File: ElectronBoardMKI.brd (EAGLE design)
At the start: 88.9 x 202.9 mm, 36 parts, among them IC1 7805TV, Q1 TN0602N3, Q2 TN0602N3, T2 2N2222, T3 2N2222, T4 2N2222

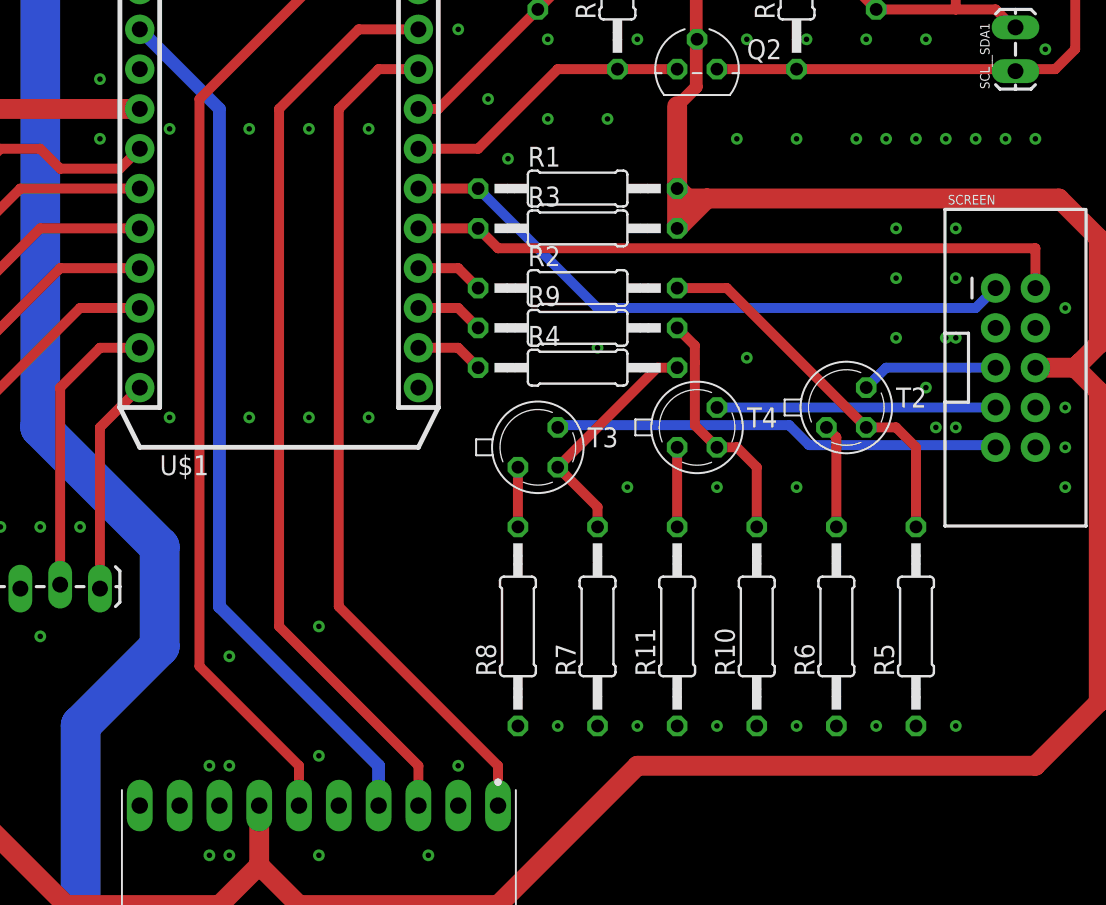
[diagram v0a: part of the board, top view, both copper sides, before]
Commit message: Net Lables + Pull-Down Resistors on Electron
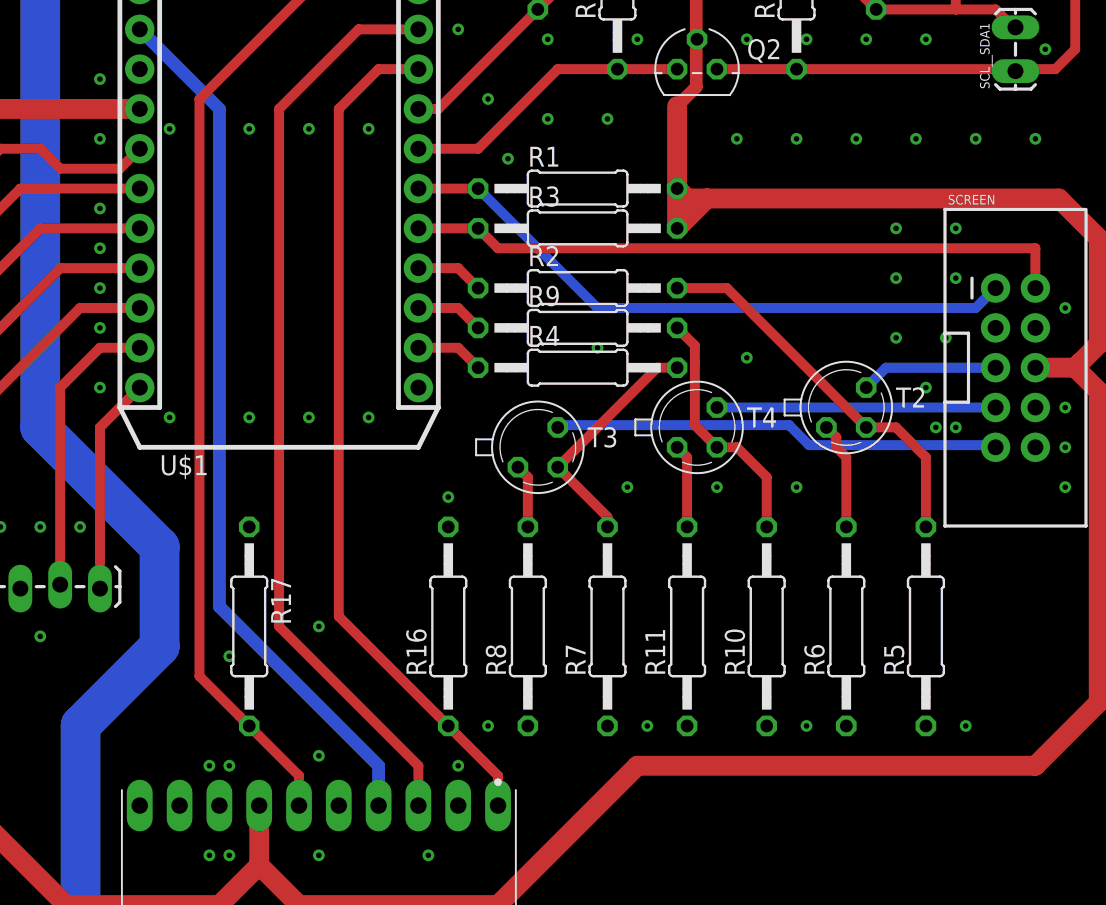
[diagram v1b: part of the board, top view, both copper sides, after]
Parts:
- added R16, R17: 47k, resistor:0207/12
- moved R10 0.64 mm to (64.1, 66.0)
- moved R5 0.64 mm to (74.3, 66.0)
- moved R6 0.64 mm to (69.2, 66.0)
- moved R8 0.64 mm to (48.9, 66.0)
- moved R11 0.63 mm to (59.1, 66.0)
- moved R7 0.63 mm to (54.0, 66.0)
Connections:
- net N$10 renamed COOLING-OUTB
- net N$11 renamed BLUE-NPN-BASE
- net N$12 renamed BLUE-NPN-EMITTER
- net N$13 renamed RED-NPN-BASE
- net N$14 renamed RED-NPN-EMITTER
- net N$15 renamed GREEN-NPN-BASE
- net N$16 renamed GREEN-NPN-EMITTER
- net N$9 renamed COOLING-OUTA
- net COOLING-INA: now also R16.1
- net COOLING-INB: now also R17.2
- net GND: now also R16.2, R17.1
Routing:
- net COOLING-INB: track 64.6 -> 65.5 mm

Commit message: Holes
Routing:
- net 3V3: track 337.0 -> 333.2 mm
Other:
- board size 88.9 x 202.9 mm -> 88 x 202.9 mm
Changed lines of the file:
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@@
 <setting verticaltext="up"/>
 </settings>
-<grid distance="0.025" unitdist="inch" unit="inch" style="lines" multiple="1" display="no" altdistance="5" altunitdist="mil" altunit="mil"/>
+<grid distance="25" unitdist="mil" unit="mil" style="lines" multiple="1" display="no" altdistance="5" altunitdist="mil" altunit="mil"/>
 <layers>
 <layer number="1" name="Top" color="4" fill="1" visible="yes" active="yes"/>
@@
 <layer number="43" name="vRestrict" color="2" fill="10" visible="yes" active="yes"/>
 <layer number="44" name="Drills" color="7" fill="1" visible="no" active="yes"/>
-<layer number="45" name="Holes" color="7" fill="1" visible="no" active="yes"/>
+<layer number="45" name="Holes" color="7" fill="1" visible="yes" active="yes"/>
 <layer number="46" name="Milling" color="3" fill="1" visible="no" active="yes"/>
 <layer number="47" name="Measures" color="7" fill="1" visible="no" active="yes"/>
@@
 <board>
 <plain>
-<wire x1="0" y1="0" x2="88.88" y2="0" width="0" layer="20"/>
-<wire x1="88.88" y1="0" x2="88.88" y2="202.87" width="0" layer="20"/>
-<wire x1="88.88" y1="202.87" x2="0" y2="202.87" width="0" layer="20"/>
+<wire x1="0" y1="0" x2="88" y2="0" width="0" layer="20"/>
+<wire x1="88" y1="0" x2="88" y2="200" width="0" layer="20"/>
+<wire x1="88" y1="200" x2="0" y2="202.87" width="0" layer="20"/>
 <wire x1="0" y1="202.87" x2="0" y2="0" width="0" layer="20"/>
+<hole x="6.15" y="6.15" drill="4"/>
+<hole x="78.05" y="6.15" drill="4"/>
+<hole x="6.15" y="193.85" drill="4"/>
+<hole x="78.05" y="193.85" drill="4"/>
+<hole x="6.15" y="150" drill="4"/>
+<hole x="78.05" y="150" drill="4"/>
 </plain>
 <attributes>
@@
 <via x="72.39" y="91.44" extent="1-16" drill="0.35"/>
 <via x="75.565" y="84.455" extent="1-16" drill="0.35"/>
-<via x="83.185" y="86.36" extent="1-16" drill="0.35"/>
-<via x="83.185" y="74.93" extent="1-16" drill="0.35"/>
-<via x="83.185" y="77.47" extent="1-16" drill="0.35"/>
-<via x="83.185" y="80.01" extent="1-16" drill="0.35"/>
+<via x="82.8675" y="86.36" extent="1-16" drill="0.35"/>
+<via x="82.8675" y="74.93" extent="1-16" drill="0.35"/>
+<via x="82.8675" y="77.47" extent="1-16" drill="0.35"/>
+<via x="82.8675" y="80.01" extent="1-16" drill="0.35"/>
 <via x="76.835" y="59.69" extent="1-16" drill="0.35"/>
 <via x="66.675" y="59.69" extent="1-16" drill="0.35"/>
@@
 <via x="24.13" y="45.72" extent="1-16" drill="0.35"/>
 <via x="39.37" y="45.72" extent="1-16" drill="0.35"/>
-<via x="3.175" y="86.36" extent="1-16" drill="0.35"/>
+<via x="3.175" y="87.63" extent="1-16" drill="0.35"/>
 <via x="1.905" y="96.52" extent="1-16" drill="0.35"/>
 <via x="1.905" y="109.855" extent="1-16" drill="0.35"/>
@@
 <wire x1="2.54" y1="106.68" x2="2.54" y2="99.06" width="1.27" layer="1"/>
 <wire x1="2.54" y1="99.06" x2="5.08" y2="96.52" width="1.27" layer="1"/>
-<wire x1="5.08" y1="96.52" x2="7.62" y2="96.52" width="1.27" layer="1"/>
+<wire x1="6.35" y1="96.52" x2="7.62" y2="96.52" width="1.27" layer="1"/>
 <wire x1="3.81" y1="110.49" x2="5.08" y2="109.22" width="1.27" layer="16"/>
 <wire x1="5.08" y1="109.22" x2="7.62" y2="109.22" width="1.27" layer="16"/>
@@
 <wire x1="31.75" y1="50.8" x2="34.29" y2="48.26" width="1.27" layer="1"/>
 <wire x1="34.29" y1="48.26" x2="46.99" y2="48.26" width="1.27" layer="1"/>
-<wire x1="55.88" y1="57.15" x2="81.28" y2="57.15" width="1.27" layer="1"/>
-<wire x1="85.324" y1="61.194" x2="81.28" y2="57.15" width="1.27" layer="1"/>
-<wire x1="46.99" y1="48.26" x2="55.88" y2="57.15" width="1.27" layer="1"/>
-<wire x1="85.324" y1="90.805" x2="82.784" y2="93.345" width="1.27" layer="1"/>
+<wire x1="54.61" y1="55.88" x2="76.2" y2="55.88" width="1.27" layer="1"/>
+<wire x1="84.689" y1="64.369" x2="76.2" y2="55.88" width="1.27" layer="1"/>
+<wire x1="46.99" y1="48.26" x2="54.61" y2="55.88" width="1.27" layer="1"/>
+<wire x1="84.689" y1="91.44" x2="82.784" y2="93.345" width="1.27" layer="1"/>
 <wire x1="82.784" y1="93.345" x2="60.325" y2="93.345" width="1.27" layer="1"/>
 <wire x1="60.325" y1="93.345" x2="58.42" y2="91.44" width="1.27" layer="1"/>
 <wire x1="58.42" y1="93.98" x2="59.055" y2="93.345" width="1.27" layer="1"/>
 <wire x1="59.055" y1="93.345" x2="60.325" y2="93.345" width="1.27" layer="1"/>
-<wire x1="81.28" y1="82.55" x2="83.82" y2="82.55" width="1.27" layer="1"/>
-<wire x1="85.324" y1="84.054" x2="85.324" y2="90.805" width="1.27" layer="1"/>
-<wire x1="84.1375" y1="82.8675" x2="85.324" y2="84.054" width="1.27" layer="1"/>
-<wire x1="83.82" y1="82.55" x2="85.324" y2="81.046" width="1.27" layer="1"/>
-<wire x1="85.324" y1="81.046" x2="85.324" y2="61.194" width="1.27" layer="1"/>
-<wire x1="83.82" y1="82.55" x2="84.1375" y2="82.8675" width="1.27" layer="1"/>
+<wire x1="84.689" y1="84.054" x2="84.689" y2="91.44" width="1.27" layer="1"/>
+<wire x1="83.5025" y1="82.8675" x2="84.689" y2="84.054" width="1.27" layer="1"/>
+<wire x1="83.185" y1="82.55" x2="84.689" y2="81.046" width="1.27" layer="1"/>
+<wire x1="84.689" y1="81.046" x2="84.689" y2="64.369" width="1.27" layer="1"/>
+<wire x1="81.28" y1="82.55" x2="83.185" y2="82.55" width="1.27" layer="1"/>
+<wire x1="5.08" y1="96.52" x2="6.35" y2="96.52" width="1.27" layer="1"/>
 </signal>
 <signal name="SCL-3V3">

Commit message: Straightened Board
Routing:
- net 3V3: track 333.2 -> 332.6 mm
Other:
- board size 88 x 202.9 mm -> 88 x 200 mm
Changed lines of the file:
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@@
 <setting verticaltext="up"/>
 </settings>
-<grid distance="25" unitdist="mil" unit="mil" style="lines" multiple="1" display="no" altdistance="5" altunitdist="mil" altunit="mil"/>
+<grid distance="12.5" unitdist="mil" unit="mil" style="lines" multiple="1" display="no" altdistance="5" altunitdist="mil" altunit="mil"/>
 <layers>
 <layer number="1" name="Top" color="4" fill="1" visible="yes" active="yes"/>
@@
 <wire x1="0" y1="0" x2="88" y2="0" width="0" layer="20"/>
 <wire x1="88" y1="0" x2="88" y2="200" width="0" layer="20"/>
-<wire x1="88" y1="200" x2="0" y2="202.87" width="0" layer="20"/>
-<wire x1="0" y1="202.87" x2="0" y2="0" width="0" layer="20"/>
+<wire x1="88" y1="200" x2="0" y2="200" width="0" layer="20"/>
+<wire x1="0" y1="200" x2="0" y2="0" width="0" layer="20"/>
 <hole x="6.15" y="6.15" drill="4"/>
 <hole x="78.05" y="6.15" drill="4"/>
@@
 <via x="10.16" y="113.665" extent="1-16" drill="0.35"/>
 <via x="5.715" y="115.57" extent="1-16" drill="0.35"/>
-<via x="5.08" y="101.6" extent="1-16" drill="0.35"/>
+<via x="5.3975" y="101.6" extent="1-16" drill="0.35"/>
 <via x="31.115" y="79.375" extent="1-16" drill="0.35"/>
 <via x="34.925" y="97.79" extent="1-16" drill="0.35"/>
@@
 <via x="24.13" y="45.72" extent="1-16" drill="0.35"/>
 <via x="39.37" y="45.72" extent="1-16" drill="0.35"/>
-<via x="3.175" y="87.63" extent="1-16" drill="0.35"/>
+<via x="4.1275" y="87.9475" extent="1-16" drill="0.35"/>
 <via x="1.905" y="96.52" extent="1-16" drill="0.35"/>
 <via x="1.905" y="109.855" extent="1-16" drill="0.35"/>
@@
 <wire x1="59.6392" y1="100.4599875" x2="59.6392" y2="109.8042" width="0.8128" layer="1"/>
 <wire x1="58.42" y1="93.98" x2="58.42" y2="91.44" width="1.27" layer="1"/>
-<wire x1="3.81" y1="110.49" x2="3.81" y2="132.08" width="1.27" layer="16"/>
-<wire x1="7.62" y1="109.22" x2="5.08" y2="109.22" width="1.27" layer="1"/>
-<wire x1="5.08" y1="109.22" x2="2.54" y2="106.68" width="1.27" layer="1"/>
-<wire x1="2.54" y1="106.68" x2="2.54" y2="99.06" width="1.27" layer="1"/>
-<wire x1="2.54" y1="99.06" x2="5.08" y2="96.52" width="1.27" layer="1"/>
+<wire x1="3.4925" y1="110.49" x2="3.4925" y2="131.7625" width="1.27" layer="16"/>
+<wire x1="7.62" y1="109.22" x2="5.3975" y2="109.22" width="1.27" layer="1"/>
+<wire x1="5.3975" y1="109.22" x2="3.4925" y2="107.315" width="1.27" layer="1"/>
+<wire x1="3.4925" y1="107.315" x2="3.4925" y2="98.1075" width="1.27" layer="1"/>
+<wire x1="3.4925" y1="98.1075" x2="5.08" y2="96.52" width="1.27" layer="1"/>
 <wire x1="6.35" y1="96.52" x2="7.62" y2="96.52" width="1.27" layer="1"/>
-<wire x1="3.81" y1="110.49" x2="5.08" y2="109.22" width="1.27" layer="16"/>
-<wire x1="5.08" y1="109.22" x2="7.62" y2="109.22" width="1.27" layer="16"/>
-<wire x1="3.81" y1="132.08" x2="6.35" y2="134.62" width="1.27" layer="16"/>
+<wire x1="3.4925" y1="110.49" x2="4.7625" y2="109.22" width="1.27" layer="16"/>
+<wire x1="4.7625" y1="109.22" x2="7.62" y2="109.22" width="1.27" layer="16"/>
+<wire x1="3.4925" y1="131.7625" x2="6.35" y2="134.62" width="1.27" layer="16"/>
 <wire x1="6.35" y1="134.62" x2="31.75" y2="134.62" width="1.27" layer="16"/>
 <wire x1="31.75" y1="134.62" x2="41.91" y2="124.46" width="1.27" layer="16"/>
@@
 <wire x1="84.689" y1="81.046" x2="84.689" y2="64.369" width="1.27" layer="1"/>
 <wire x1="81.28" y1="82.55" x2="83.185" y2="82.55" width="1.27" layer="1"/>
-<wire x1="5.08" y1="96.52" x2="6.35" y2="96.52" width="1.27" layer="1"/>
+<wire x1="5.3975" y1="96.52" x2="6.35" y2="96.52" width="1.27" layer="1"/>
+<wire x1="5.08" y1="96.52" x2="5.3975" y2="96.52" width="1.27" layer="1"/>
 </signal>
 <signal name="SCL-3V3">

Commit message: DRC Fixes
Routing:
- net 3V3: track 332.6 -> 328.3 mm
- net COOLING-PWM: track 60.4 -> 59.1 mm
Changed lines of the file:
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@@
 <setting verticaltext="up"/>
 </settings>
-<grid distance="12.5" unitdist="mil" unit="mil" style="lines" multiple="1" display="no" altdistance="5" altunitdist="mil" altunit="mil"/>
+<grid distance="6.25" unitdist="mil" unit="mil" style="lines" multiple="1" display="no" altdistance="5" altunitdist="mil" altunit="mil"/>
 <layers>
 <layer number="1" name="Top" color="4" fill="1" visible="yes" active="yes"/>
@@
 </class>
 </classes>
-<designrules name="default">
+<designrules name="default *">
 <description language="de">&lt;b&gt;EAGLE Design Rules&lt;/b&gt;
 &lt;p&gt;
@@
 <param name="mtCopper" value="0.035mm 0.035mm 0.035mm 0.035mm 0.035mm 0.035mm 0.035mm 0.035mm 0.035mm 0.035mm 0.035mm 0.035mm 0.035mm 0.035mm 0.035mm 0.035mm"/>
 <param name="mtIsolate" value="1.5mm 0.15mm 0.2mm 0.15mm 0.2mm 0.15mm 0.2mm 0.15mm 0.2mm 0.15mm 0.2mm 0.15mm 0.2mm 0.15mm 0.2mm"/>
-<param name="mdWireWire" value="6mil"/>
-<param name="mdWirePad" value="6mil"/>
-<param name="mdWireVia" value="6mil"/>
+<param name="mdWireWire" value="20mil"/>
+<param name="mdWirePad" value="10mil"/>
+<param name="mdWireVia" value="12.5mil"/>
 <param name="mdPadPad" value="6mil"/>
 <param name="mdPadVia" value="6mil"/>
@@
 <contactref element="C1" pad="-"/>
 <contactref element="C2" pad="-"/>
-<polygon width="1.27" layer="16" isolate="0.3048">
+<polygon width="0.127" layer="16" isolate="0.508">
 <vertex x="-19.05" y="226.06"/>
 <vertex x="-19.05" y="-26.67"/>
@@
 <vertex x="110.49" y="226.06"/>
 </polygon>
-<polygon width="1.27" layer="1" isolate="0.3048">
+<polygon width="0.127" layer="1" isolate="0.508">
 <vertex x="-7.62" y="210.82"/>
 <vertex x="-7.62" y="-13.97"/>
@@
 <via x="72.39" y="91.44" extent="1-16" drill="0.35"/>
 <via x="75.565" y="84.455" extent="1-16" drill="0.35"/>
-<via x="82.8675" y="86.36" extent="1-16" drill="0.35"/>
-<via x="82.8675" y="74.93" extent="1-16" drill="0.35"/>
-<via x="82.8675" y="77.47" extent="1-16" drill="0.35"/>
-<via x="82.8675" y="80.01" extent="1-16" drill="0.35"/>
+<via x="83.5025" y="86.36" extent="1-16" drill="0.35"/>
+<via x="83.5025" y="77.47" extent="1-16" drill="0.35"/>
+<via x="83.5025" y="80.01" extent="1-16" drill="0.35"/>
 <via x="76.835" y="59.69" extent="1-16" drill="0.35"/>
 <via x="66.675" y="59.69" extent="1-16" drill="0.35"/>
@@
 <via x="31.115" y="97.79" extent="1-16" drill="0.35"/>
 <via x="26.035" y="97.79" extent="1-16" drill="0.35"/>
-<via x="47.625" y="95.885" extent="1-16" drill="0.35"/>
+<via x="46.6725" y="95.5675" extent="1-16" drill="0.35"/>
 <via x="44.45" y="104.14" extent="1-16" drill="0.35"/>
 <via x="62.865" y="103.505" extent="1-16" drill="0.35"/>
@@
 <contactref element="SCREEN" pad="9"/>
 <contactref element="T3" pad="3"/>
-<wire x1="78.6003" y1="77.6097" x2="78.74" y2="77.47" width="0.635" layer="16"/>
-<wire x1="65.5718125" y1="78.8797" x2="66.8418125" y2="77.6097" width="0.635" layer="16"/>
-<wire x1="66.8418125" y1="77.6097" x2="78.6003" y2="77.6097" width="0.635" layer="16"/>
-<wire x1="65.5718125" y1="78.8797" x2="50.9397" y2="78.8797" width="0.635" layer="16"/>
-<wire x1="50.9397" y1="78.8797" x2="50.8" y2="78.74" width="0.635" layer="16"/>
+<wire x1="65.2543125" y1="78.72095" x2="66.6830625" y2="77.2922" width="0.635" layer="16"/>
+<wire x1="66.6830625" y1="77.2922" x2="78.5622" y2="77.2922" width="0.635" layer="16"/>
+<wire x1="65.2543125" y1="78.72095" x2="50.81905" y2="78.72095" width="0.635" layer="16"/>
+<wire x1="50.81905" y1="78.72095" x2="50.8" y2="78.74" width="0.635" layer="16"/>
+<wire x1="78.5622" y1="77.2922" x2="78.74" y2="77.47" width="0.635" layer="16"/>
 </signal>
 <signal name="SCREEN-GREEN">
@@
 <contactref element="R3" pad="1"/>
 <wire x1="41.91" y1="91.44" x2="45.72" y2="91.44" width="0.635" layer="1"/>
-<wire x1="45.72" y1="91.44" x2="46.99" y2="90.17" width="0.635" layer="1"/>
-<wire x1="46.99" y1="90.17" x2="81.28" y2="90.17" width="0.635" layer="1"/>
-<wire x1="81.28" y1="90.17" x2="81.28" y2="87.63" width="0.635" layer="1"/>
+<wire x1="45.72" y1="90.805" x2="46.99" y2="89.535" width="0.635" layer="1"/>
+<wire x1="46.99" y1="89.535" x2="81.28" y2="89.535" width="0.635" layer="1"/>
+<wire x1="81.28" y1="89.535" x2="81.28" y2="87.63" width="0.635" layer="1"/>
+<wire x1="45.72" y1="91.44" x2="45.72" y2="90.805" width="0.635" layer="1"/>
 </signal>
 <signal name="SCREEN-SCL">
@@
 <contactref element="U$2" pad="PWM"/>
 <contactref element="U$1" pad="28"/>
-<wire x1="41.91" y1="54.61" x2="41.91" y2="55.88" width="0.635" layer="1"/>
-<wire x1="41.91" y1="54.61" x2="41.91" y2="57.15" width="0.635" layer="1"/>
+<wire x1="41.91" y1="55.88" x2="41.91" y2="57.15" width="0.635" layer="1"/>
 <wire x1="41.91" y1="57.15" x2="33.02" y2="66.04" width="0.635" layer="1"/>
 <wire x1="33.02" y1="66.04" x2="33.02" y2="99.06" width="0.635" layer="1"/>
 <wire x1="33.02" y1="99.06" x2="38.1" y2="104.14" width="0.635" layer="1"/>
 <wire x1="38.1" y1="104.14" x2="41.91" y2="104.14" width="0.635" layer="1"/>
+<wire x1="41.91" y1="54.61" x2="41.91" y2="55.88" width="0.635" layer="1"/>
 </signal>
 <signal name="COOLING-INA">
@@
 <wire x1="64.135" y1="75.565" x2="64.135" y2="72.39" width="0.635" layer="1"/>
 <wire x1="60.96" y1="77.47" x2="62.23" y2="77.47" width="0.635" layer="1"/>
-<wire x1="58.42" y1="85.09" x2="59.5503" y2="83.9597" width="0.635" layer="1"/>
-<wire x1="59.5503" y1="83.9597" x2="59.5503" y2="82.8784875" width="0.635" layer="1"/>
+<wire x1="58.7375" y1="85.09" x2="59.8678" y2="83.9597" width="0.635" layer="1"/>
+<wire x1="59.8678" y1="83.9597" x2="59.8678" y2="81.9259875" width="0.635" layer="1"/>
 <wire x1="59.5503" y1="78.8797" x2="60.96" y2="77.47" width="0.635" layer="1"/>
-<wire x1="59.5503" y1="82.8784875" x2="59.5503" y2="78.8797" width="0.635" layer="1"/>
+<wire x1="59.5503" y1="81.6084875" x2="59.5503" y2="78.8797" width="0.635" layer="1"/>
+<wire x1="58.42" y1="85.09" x2="58.7375" y2="85.09" width="0.635" layer="1"/>
+<wire x1="59.8678" y1="81.9259875" x2="59.5503" y2="81.6084875" width="0.635" layer="1"/>
 </signal>
 <signal name="GREEN-NPN-EMITTER">
@@
 <wire x1="55.88" y1="114.3" x2="59.69" y2="109.855" width="1.27" layer="1"/>
 <wire x1="59.69" y1="103.505" x2="59.69" y2="109.855" width="0.635" layer="1"/>
-<wire x1="58.42" y1="93.98" x2="58.42" y2="99.2407875" width="1.27" layer="1"/>
+<wire x1="58.26125" y1="94.13875" x2="58.26125" y2="97.8056875" width="0.635" layer="1"/>
 <wire x1="59.6392" y1="109.8042" x2="59.69" y2="109.855" width="0.8128" layer="1"/>
-<wire x1="58.42" y1="99.2407875" x2="59.6392" y2="100.4599875" width="0.8128" layer="1"/>
-<wire x1="59.6392" y1="100.4599875" x2="59.6392" y2="109.8042" width="0.8128" layer="1"/>
+<wire x1="58.26125" y1="97.8056875" x2="59.6519" y2="99.1963375" width="0.635" layer="1"/>
 <wire x1="58.42" y1="93.98" x2="58.42" y2="91.44" width="1.27" layer="1"/>
 <wire x1="3.4925" y1="110.49" x2="3.4925" y2="131.7625" width="1.27" layer="16"/>
@@
 <wire x1="34.29" y1="48.26" x2="46.99" y2="48.26" width="1.27" layer="1"/>
 <wire x1="54.61" y1="55.88" x2="76.2" y2="55.88" width="1.27" layer="1"/>
-<wire x1="84.689" y1="64.369" x2="76.2" y2="55.88" width="1.27" layer="1"/>
+<wire x1="85.324" y1="65.004" x2="76.2" y2="55.88" width="1.27" layer="1"/>
 <wire x1="46.99" y1="48.26" x2="54.61" y2="55.88" width="1.27" layer="1"/>
-<wire x1="84.689" y1="91.44" x2="82.784" y2="93.345" width="1.27" layer="1"/>
-<wire x1="82.784" y1="93.345" x2="60.325" y2="93.345" width="1.27" layer="1"/>
+<wire x1="85.324" y1="91.44" x2="83.419" y2="93.345" width="1.27" layer="1"/>
+<wire x1="83.419" y1="93.345" x2="60.325" y2="93.345" width="1.27" layer="1"/>
 <wire x1="60.325" y1="93.345" x2="58.42" y2="91.44" width="1.27" layer="1"/>
 <wire x1="58.42" y1="93.98" x2="59.055" y2="93.345" width="1.27" layer="1"/>
 <wire x1="59.055" y1="93.345" x2="60.325" y2="93.345" width="1.27" layer="1"/>
-<wire x1="84.689" y1="84.054" x2="84.689" y2="91.44" width="1.27" layer="1"/>
-<wire x1="83.5025" y1="82.8675" x2="84.689" y2="84.054" width="1.27" layer="1"/>
-<wire x1="83.185" y1="82.55" x2="84.689" y2="81.046" width="1.27" layer="1"/>
-<wire x1="84.689" y1="81.046" x2="84.689" y2="64.369" width="1.27" layer="1"/>
-<wire x1="81.28" y1="82.55" x2="83.185" y2="82.55" width="1.27" layer="1"/>
+<wire x1="85.324" y1="84.054" x2="85.324" y2="91.44" width="1.27" layer="1"/>
+<wire x1="83.82" y1="82.55" x2="85.324" y2="84.054" width="1.27" layer="1"/>
+<wire x1="83.82" y1="82.55" x2="85.324" y2="81.046" width="1.27" layer="1"/>
+<wire x1="85.324" y1="81.046" x2="85.324" y2="65.004" width="1.27" layer="1"/>
+<wire x1="81.28" y1="82.55" x2="83.82" y2="82.55" width="1.27" layer="1"/>
 <wire x1="5.3975" y1="96.52" x2="6.35" y2="96.52" width="1.27" layer="1"/>
 <wire x1="5.08" y1="96.52" x2="5.3975" y2="96.52" width="1.27" layer="1"/>
+<wire x1="59.6519" y1="99.1963375" x2="59.6519" y2="103.380275" width="0.635" layer="1"/>
+<wire x1="58.42" y1="93.98" x2="58.26125" y2="94.13875" width="1.27" layer="1"/>
 </signal>
 <signal name="SCL-3V3">
